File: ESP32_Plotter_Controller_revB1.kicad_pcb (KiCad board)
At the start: 2 copper layers, 99.1 x 55.4 mm, 53 parts, among them J1 ARM JTAG 10pin, J10 Pen Lift, J11 Vselect, J12 X Motor, J13 Y Motor, J14 Neo Pixel LEDs, J15 Pen Direction, J16 Aux Port (I2C), J17 USB_C_Receptacle_USB2.0, J18 E-Stop, J19 Y Limit Switch, J2 Power, J3 5V Aux, J4 Vin Aux, J5 X Limit Switch, J6 Aux Port (SPI), J7 X Limit, J8 Micro_SD_Card, J9 Y Limit, SW1 RESET, SW2 BOOT, U1 ESP32-WROOM-32D, U2 TMC2130, U3 TMC2130, U4 XL1509, U5 CH340C, U6 AMS1117-3.3

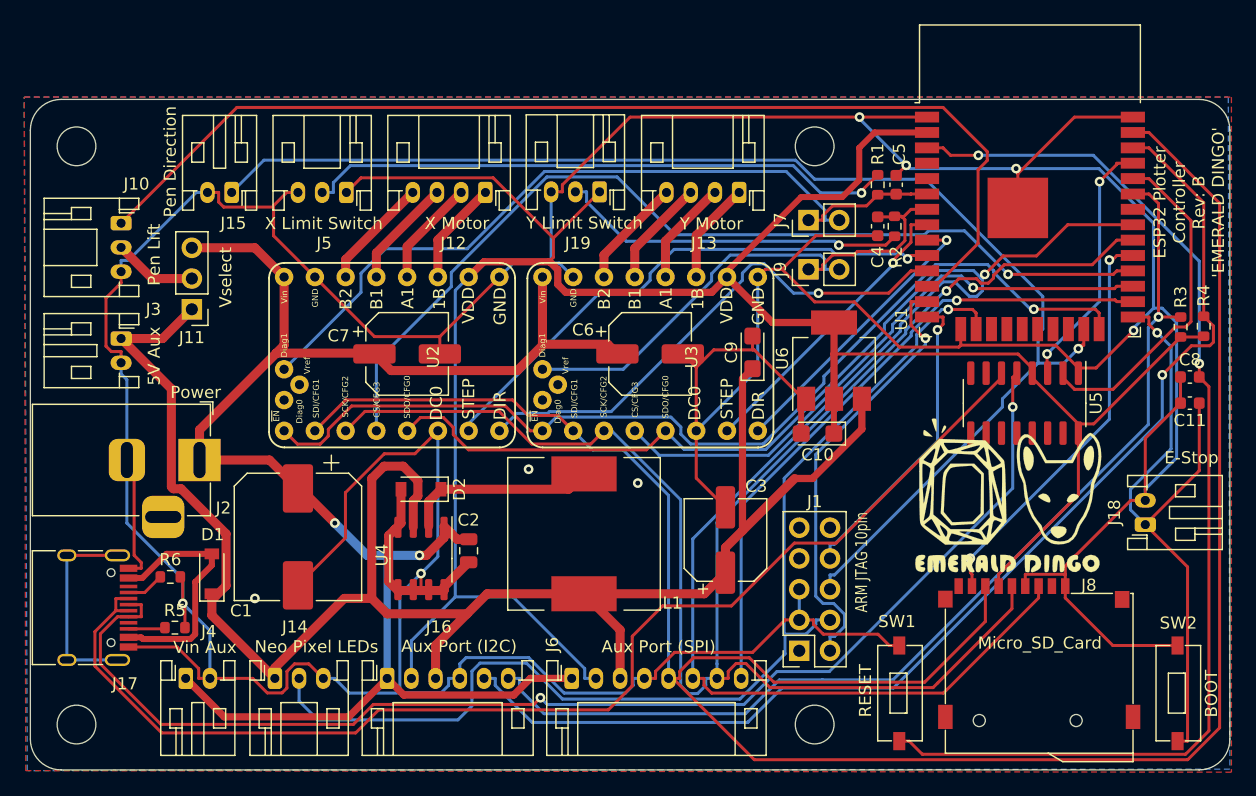
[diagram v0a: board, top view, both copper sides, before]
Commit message: Fix SD card footprint and add pull-up resistors
Rev B was using an old and incorrect footprint causing a 3.3v short to ground when an SD card was inserted. Update to use the fixed footprint.

Added pull-up resistors for EN and IO0 (Boot mode). On test board, IO0 appeared to be pulled permanently low. It could be programmed but would not boot. It may only be necessary for EN to be pulled high but added the pull-up for IO0 just incase.
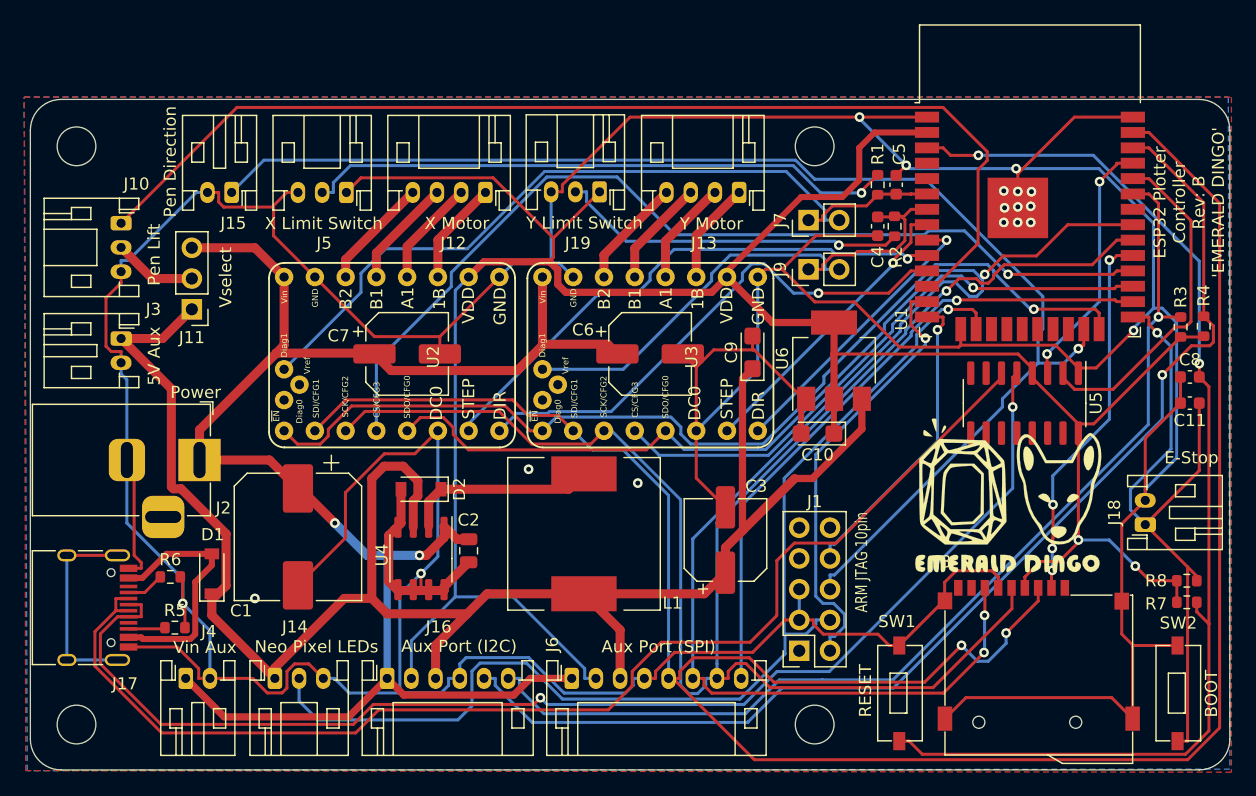
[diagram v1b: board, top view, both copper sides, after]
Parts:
- added R7: 10k, Resistor_SMD:R_0603_1608Metric, F.Cu at (120.9, 110.6)
- added R8: 10k, Resistor_SMD:R_0603_1608Metric, F.Cu at (120.9, 108.8)
- J8: value Micro_SD_Card -> Micro_SD_Card_TF-01A
- moved J8 0.15 mm to (100.9, 109.4)
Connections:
- J8 pad 10: (no net) -> GND
- J8 pad 11: (no net) -> GND
- J8 pad 12: (no net) -> GND
- J8 pad 13: (no net) -> GND
- J8 pad 9: GND -> Net-(J8-Pad9)
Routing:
- net GND: track 487.4 -> 513.3 mm, vias 9 -> 18
- net +3V3: track 196.7 -> 208.1 mm, vias 0 -> 2
- net /MOSI: track 183.6 -> 188.4 mm, vias 0 -> 2
- net /CS_SD: track 33.8 -> 31.2 mm, vias 2 -> 4
- net /EN: track 92.3 -> 94.5 mm
- net /MISO: track 151.6 -> 149.9 mm, vias 1 -> 3
- net /IO0: track 53.2 -> 54.6 mm
- net Net-(J17-PadA7): track 100.5 -> 101.4 mm

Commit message: Add pull-ups and manually tweak some routes
Added pull-ups for EN, Bpot, X_Limit & Y_Limit.
Re-routed some tracks to improve thermal ground on ESP32 module and to allow for better Gnd fills.
Regenerated Gerber files to include footprint values on front silkscreen.
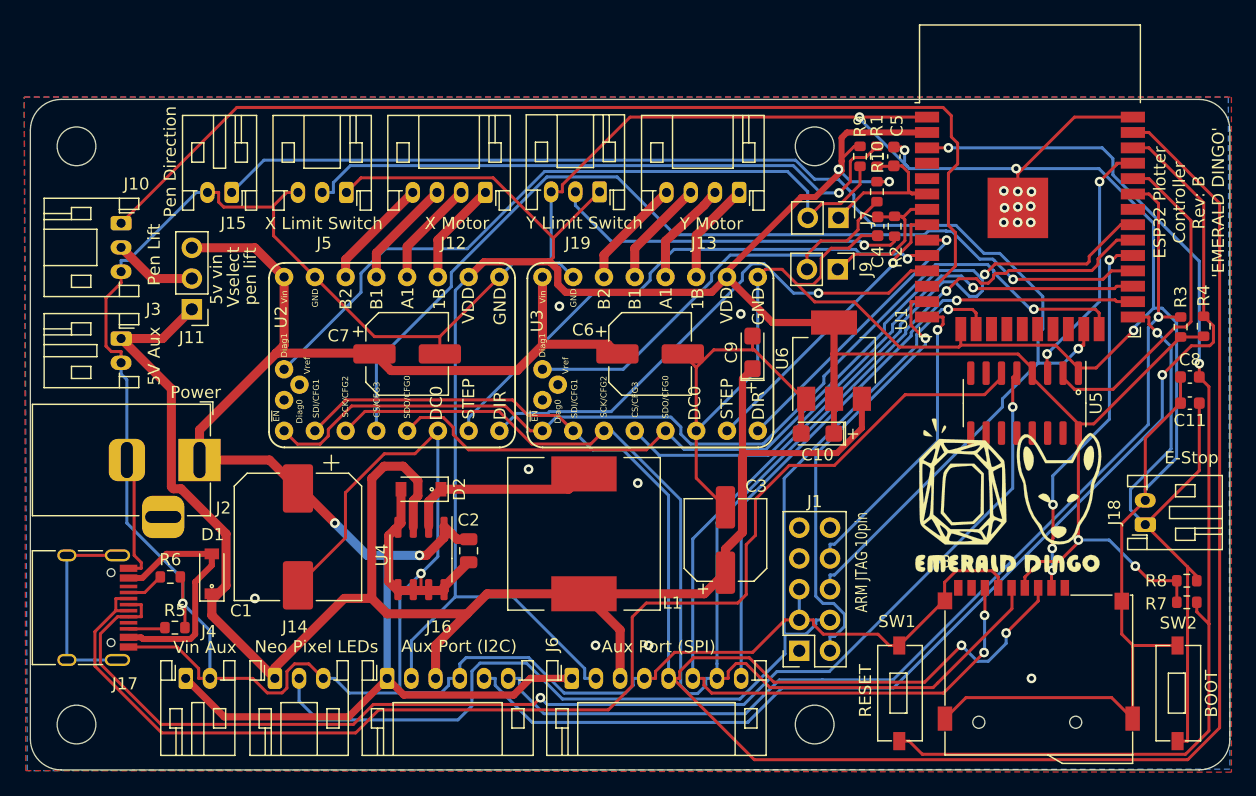
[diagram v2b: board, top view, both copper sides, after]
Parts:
- added R10: 10K, Resistor_SMD:R_0603_1608Metric, F.Cu at (95.3, 76.6)
- added R9: 10K, Resistor_SMD:R_0603_1608Metric, F.Cu at (93.9, 73.7)
- moved J7 2.48 mm to (92.1, 78.8), turned to 270 degrees
- moved J9 2.41 mm to (92.1, 83.1), turned to 270 degrees
- moved R1 2.35 mm to (95.3, 73.7)
- moved C5 2.34 mm to (96.7, 73.7)
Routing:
- net +3V3: track 208.1 -> 216.2 mm, vias 2 -> 4
- net Net-(J9-Pad2): track 29.7 -> 36.5 mm
- net Net-(J7-Pad2): track 55.7 -> 60.7 mm
- net +5V: track 153.3 -> 148.7 mm
- net Net-(J17-PadA7): track 101.4 -> 105.6 mm
- net /X_Limit: track 10.9 -> 14.3 mm
- net /Y_Limit: track 15.6 -> 12.9 mm
- net Net-(J5-Pad2): track 48.9 -> 50.7 mm
- net /PEN_LIFT: track 90.6 -> 89.0 mm
- net GND: track 513.3 -> 514.7 mm, vias 18 -> 23
- net /EN: track 94.5 -> 95.3 mm
- net /PEN_DIR_JTAG_TDO: track 110.1 -> 110.7 mm
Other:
- board text added: "5v vin"
- board text added: "pen lift"

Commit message: Silkscreen tweaks and remove unnecessary tracks from USB-C connector shield
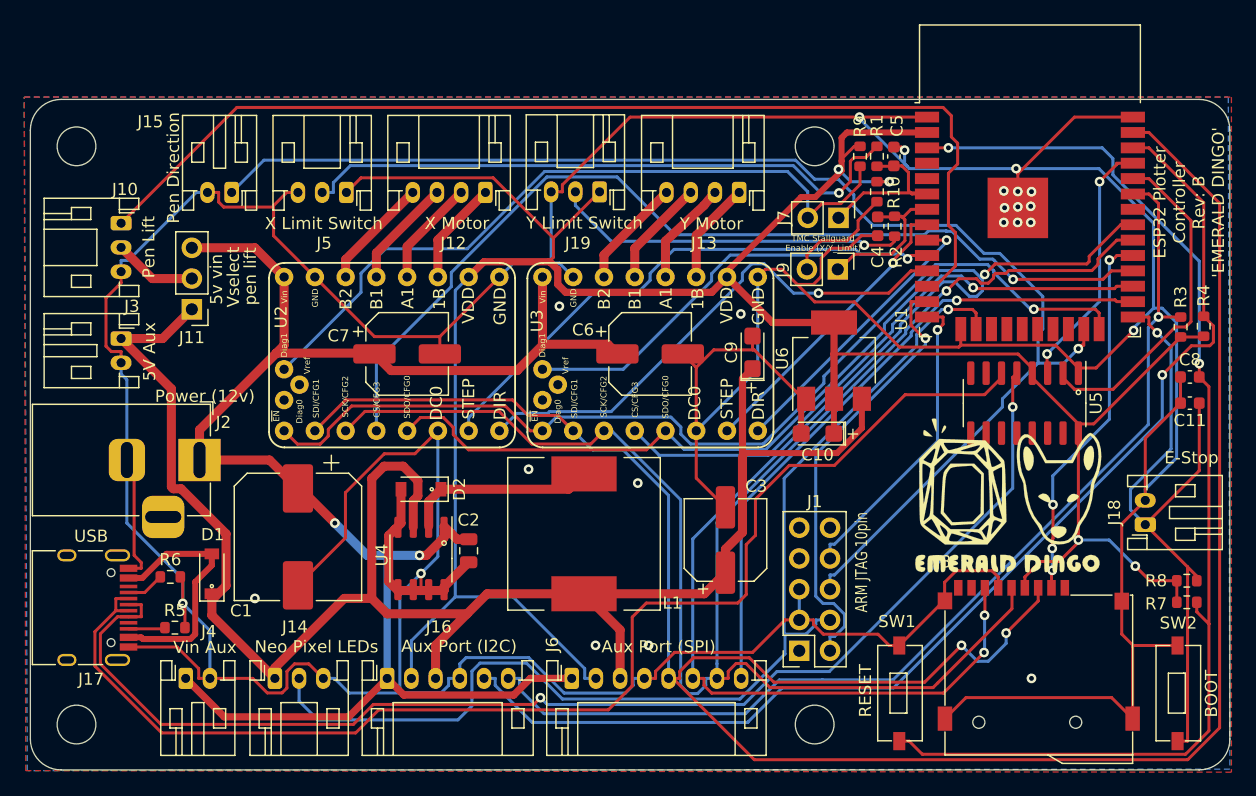
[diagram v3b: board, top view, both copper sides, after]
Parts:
- J2: value Power -> Power (12v)
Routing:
- net Net-(J17-PadS1): track 17.0 -> 0.00 mm
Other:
- board text added: "TMC Stallguard Enable (X/Y_Limit)"
- board text added: "USB"
